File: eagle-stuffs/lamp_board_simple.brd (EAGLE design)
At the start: 44.1 x 44.4 mm, 7 parts

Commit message: Ajustements to silk
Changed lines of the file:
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@@
 <grid distance="0.05" unitdist="inch" unit="inch" style="lines" multiple="1" display="yes" altdistance="0.025" altunitdist="inch" altunit="inch"/>
 <layers>
-<layer number="1" name="Top" color="4" fill="1" visible="yes" active="yes"/>
-<layer number="16" name="Bottom" color="1" fill="1" visible="yes" active="yes"/>
+<layer number="1" name="Top" color="4" fill="1" visible="no" active="yes"/>
+<layer number="16" name="Bottom" color="1" fill="1" visible="no" active="yes"/>
 <layer number="17" name="Pads" color="2" fill="1" visible="yes" active="yes"/>
 <layer number="18" name="Vias" color="2" fill="1" visible="yes" active="yes"/>
@@
 <hole x="41.91" y="2.54" drill="1.3"/>
 <hole x="2.54" y="2.54" drill="1.3"/>
-<text x="2.54" y="36.83" size="1.778" layer="26">Rev. A</text>
-<text x="15.24" y="31.75" size="1.27" layer="26">1</text>
-<text x="29.21" y="10.16" size="1.27" layer="26">1</text>
+<text x="2.54" y="36.83" size="1.778" layer="21">Rev. A</text>
+<text x="15.24" y="31.75" size="1.27" layer="21">1</text>
+<text x="29.21" y="10.16" size="1.27" layer="21">1</text>
 </plain>
 <attributes>
@@
 <elements>
 <element name="N1" library="russian-nixies" package="IN-14" value="IN-14" x="33.02" y="21.59" smashed="yes">
-<attribute name="NAME" x="40.4813" y="29.21" size="1.27" layer="25" rot="R90"/>
+<attribute name="NAME" x="23.9713" y="25.4" size="1.27" layer="25" rot="R90"/>
 </element>
 <element name="N2" library="russian-nixies" package="IN-14" value="IN-14" x="12.7" y="21.59" smashed="yes">
-<attribute name="NAME" x="4.9213" y="29.21" size="1.27" layer="25" rot="R90"/>
+<attribute name="NAME" x="3.6513" y="25.4" size="1.27" layer="25" rot="R90"/>
 </element>
 <element name="LED1" library="led" package="LED5MM" value="" x="33.02" y="21.59" smashed="yes" rot="R270">
-<attribute name="NAME" x="28.4734" y="23.495" size="1.27" layer="25" ratio="10" rot="R270"/>
+<attribute name="NAME" x="29.7434" y="24.765" size="1.27" layer="25" ratio="10"/>
 <attribute name="VALUE" x="31.2166" y="18.3896" size="1.27" layer="27" ratio="10" rot="R270"/>
 </element>
 <element name="LED2" library="led" package="LED5MM" value="" x="12.7" y="21.59" smashed="yes" rot="R270">
-<attribute name="NAME" x="10.6934" y="17.145" size="1.27" layer="25" ratio="10"/>
+<attribute name="NAME" x="9.4234" y="24.765" size="1.27" layer="25" ratio="10"/>
 <attribute name="VALUE" x="10.8966" y="18.3896" size="1.27" layer="27" ratio="10" rot="R270"/>
 </element>

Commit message: Minor ajustements
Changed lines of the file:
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@@
 <grid distance="0.05" unitdist="inch" unit="inch" style="lines" multiple="1" display="yes" altdistance="0.025" altunitdist="inch" altunit="inch"/>
 <layers>
-<layer number="1" name="Top" color="4" fill="1" visible="no" active="yes"/>
-<layer number="16" name="Bottom" color="1" fill="1" visible="no" active="yes"/>
+<layer number="1" name="Top" color="4" fill="1" visible="yes" active="yes"/>
+<layer number="16" name="Bottom" color="1" fill="1" visible="yes" active="yes"/>
 <layer number="17" name="Pads" color="2" fill="1" visible="yes" active="yes"/>
 <layer number="18" name="Vias" color="2" fill="1" visible="yes" active="yes"/>
@@
 <wire x1="44.12" y1="44.44" x2="0" y2="44.44" width="0" layer="20"/>
 <wire x1="0" y1="44.44" x2="0" y2="0" width="0" layer="20"/>
-<hole x="2.54" y="41.91" drill="1.3"/>
-<hole x="41.91" y="41.91" drill="1.3"/>
-<hole x="41.91" y="2.54" drill="1.3"/>
-<hole x="2.54" y="2.54" drill="1.3"/>
+<hole x="2.54" y="41.91" drill="2.8"/>
+<hole x="41.91" y="41.91" drill="2.8"/>
+<hole x="41.91" y="2.54" drill="2.8"/>
+<hole x="2.54" y="2.54" drill="2.8"/>
 <text x="2.54" y="36.83" size="1.778" layer="21">Rev. A</text>
 <text x="15.24" y="31.75" size="1.27" layer="21">1</text>
@@
 </element>
 <element name="ANODE" library="pinhead" package="1X02/90" value="" x="2.54" y="8.89" smashed="yes" rot="R90">
-<attribute name="NAME" x="5.08" y="4.445" size="1.27" layer="25" ratio="10"/>
+<attribute name="NAME" x="3.81" y="4.445" size="1.27" layer="25" ratio="10"/>
 <attribute name="VALUE" x="6.35" y="13.335" size="1.27" layer="27" rot="R180"/>
 </element>

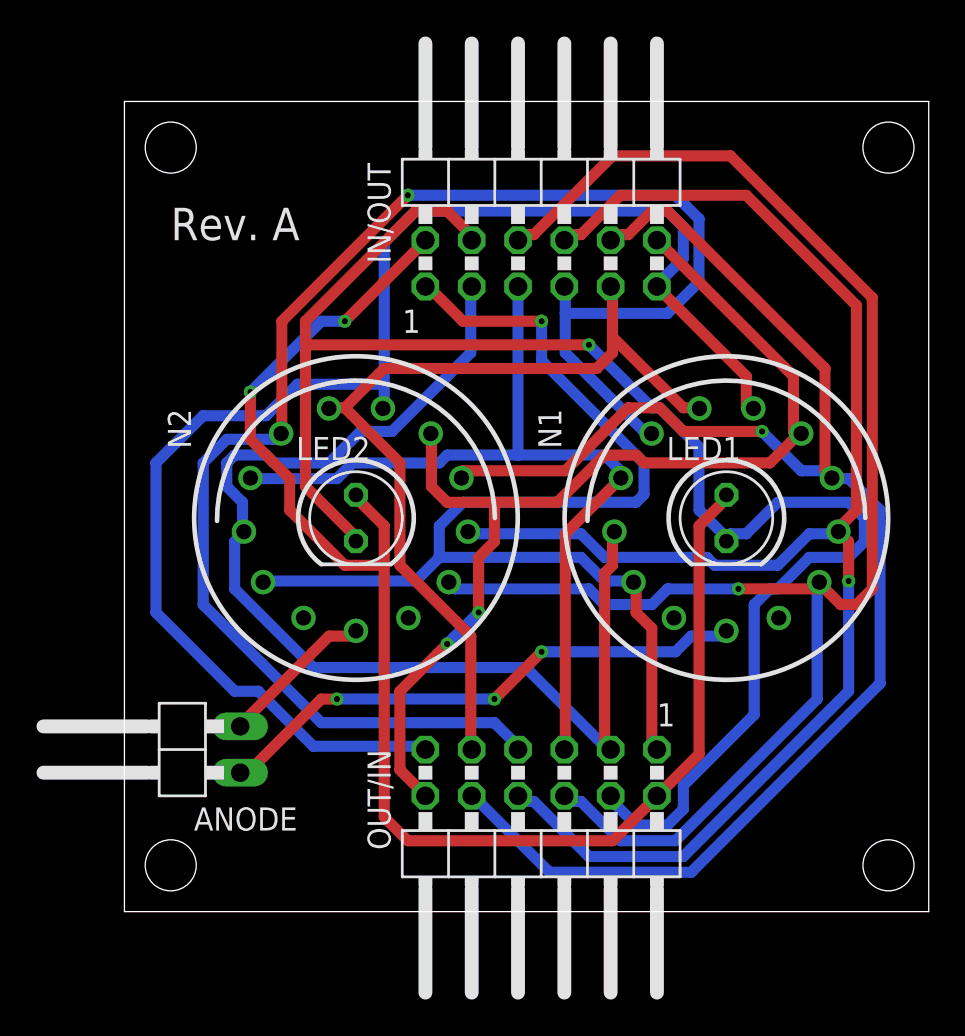
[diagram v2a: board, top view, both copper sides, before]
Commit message: Corrected mirror pinout on nixie
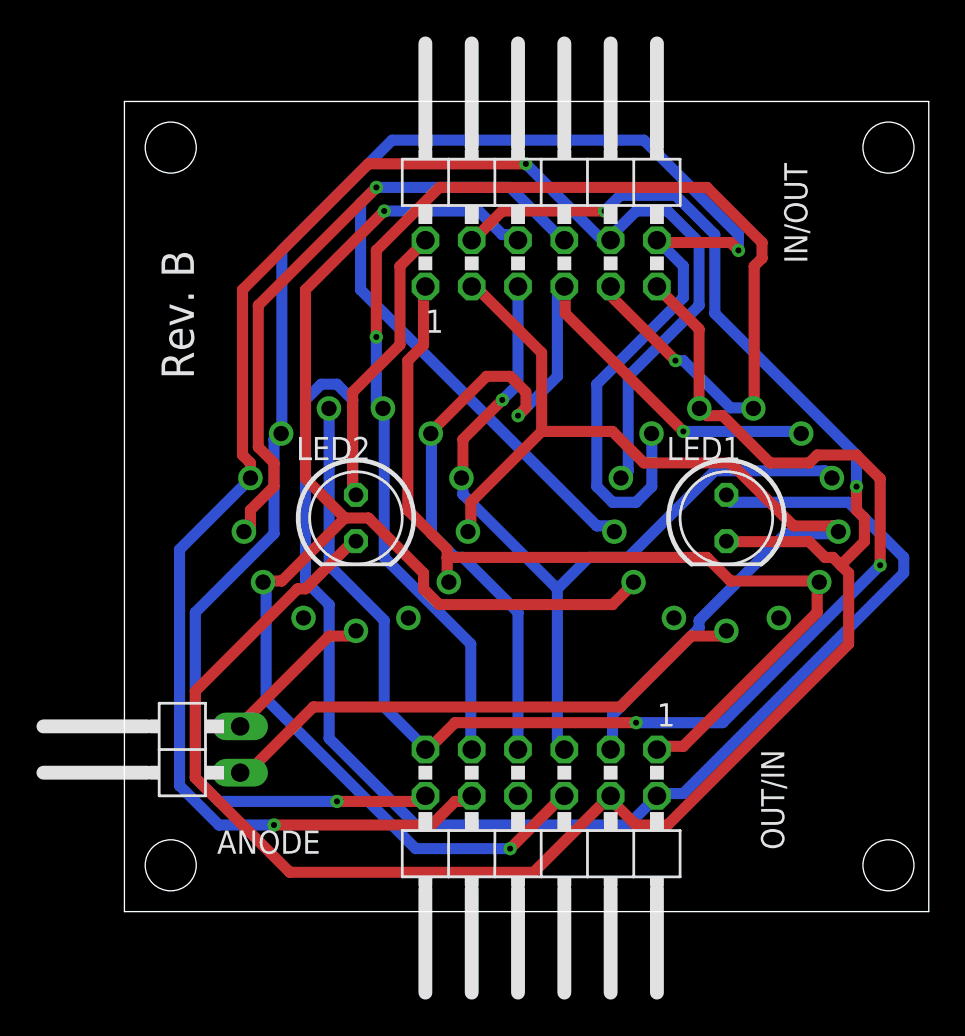
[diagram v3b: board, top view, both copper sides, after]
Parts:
- flipped N1 to the bottom
- flipped N2 to the bottom
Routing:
- net N$19: track 58.3 -> 102.3 mm
- net N$16: track 87.5 -> 53.3 mm, vias 1 -> 2
- net N$21: track 86.7 -> 59.6 mm
- net N$17: track 48.5 -> 74.1 mm, vias 0 -> 2
- net N$3: track 90.8 -> 110.2 mm, vias 1 -> 2
- net N$4: track 79.7 -> 94.8 mm, vias 2 -> 0
- net N$13: track 63.8 -> 52.1 mm, vias 1 -> 0
- net N$22: track 90.7 -> 79.9 mm, vias 1 -> 2
- net N$14: track 64.0 -> 54.0 mm
- net N$18: track 80.0 -> 74.2 mm, vias 0 -> 2
- net N$20: track 87.2 -> 92.6 mm, vias 1 -> 2
- net N$15: vias 0 -> 1
- net N$1: vias 3 -> 0
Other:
- board text added: "Rev. B"
- board text removed: "Rev. A"

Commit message: Added some info
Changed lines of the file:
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@@
 <elements>
 <element name="N1" library="russian-nixies" package="IN-14" value="IN-14" x="33.02" y="21.59" smashed="yes" rot="MR0">
-<attribute name="NAME" x="42.0687" y="25.4" size="1.27" layer="26" rot="MR90"/>
+<attribute name="NAME" x="39.5287" y="29.21" size="1.27" layer="25" rot="R90"/>
 </element>
 <element name="N2" library="russian-nixies" package="IN-14" value="IN-14" x="12.7" y="21.59" smashed="yes" rot="MR0">
-<attribute name="NAME" x="21.7487" y="25.4" size="1.27" layer="26" rot="MR90"/>
+<attribute name="NAME" x="19.2087" y="29.21" size="1.27" layer="25" rot="R90"/>
 </element>
 <element name="LED1" library="led" package="LED5MM" value="" x="33.02" y="21.59" smashed="yes" rot="R270">
@@
 </element>
 <element name="OUT/IN" library="pinhead" package="2X06/90" value="" x="22.86" y="2.54" smashed="yes" rot="R180">
-<attribute name="NAME" x="34.925" y="8.89" size="1.27" layer="25" ratio="10" rot="R270"/>
+<attribute name="NAME" x="36.195" y="8.89" size="1.27" layer="25" ratio="10" rot="R270"/>
 <attribute name="VALUE" x="13.335" y="6.35" size="1.27" layer="27" rot="R270"/>
 </element>
